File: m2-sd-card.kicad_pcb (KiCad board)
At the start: 4 copper layers, 30 x 22 mm, 16 parts, among them J101 M.2_Key_E, J102 Conn_01x02, J103 Conn_02x03_Counter_Clockwise, J104 Conn_02x03_Counter_Clockwise, J105 Conn_01x01, J106 Conn_01x03, J107 Conn_01x02, J108 USB_B_Micro, J109 Micro_SD, U101 SN74LV1T34DBV

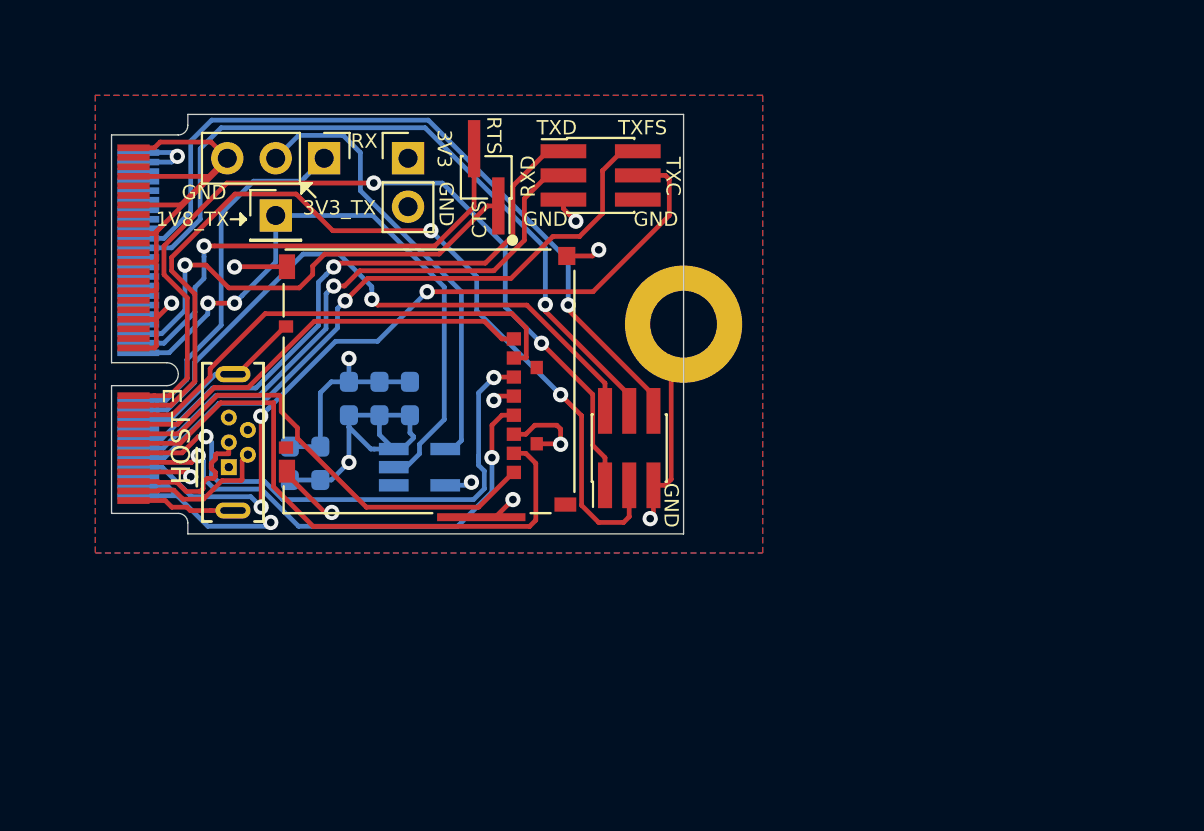
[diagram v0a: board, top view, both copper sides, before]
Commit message: Import all of the footprints into the layout
Delete the traces and footprints from the M.2 breakout board.

Update the design rules constraints and physical stackup using PCBWay's
manufacturing capabilities. These rules should work well for essentially
any manufacturer that ends up being used.

Adjust the NVT4857UK's WLCSP20 footprint according to NXP's recommended
footprint and PCBWay's manufacturing capabilities (allowing for at least
a 4mil soldermask web/bridge between pads). This package's small 0.4mm
pitch makes it so that via-in-pad technology is required for this
board's design.

Create a footprint which contains a MicroSD card 3D Step model and add
it to the board, specifying that it does not exist in the schematic.
This model is used to determine the placement of the MicroSD slot,
making sure that there is sufficient room to insert and remove the
MicroSD card while the M.2 module is installed in the phone. The current
position of x=131.8mm, y=-98.3mm for the DM3AT-SF-PEJM5 MicroSD slot allows
for this to be possible.
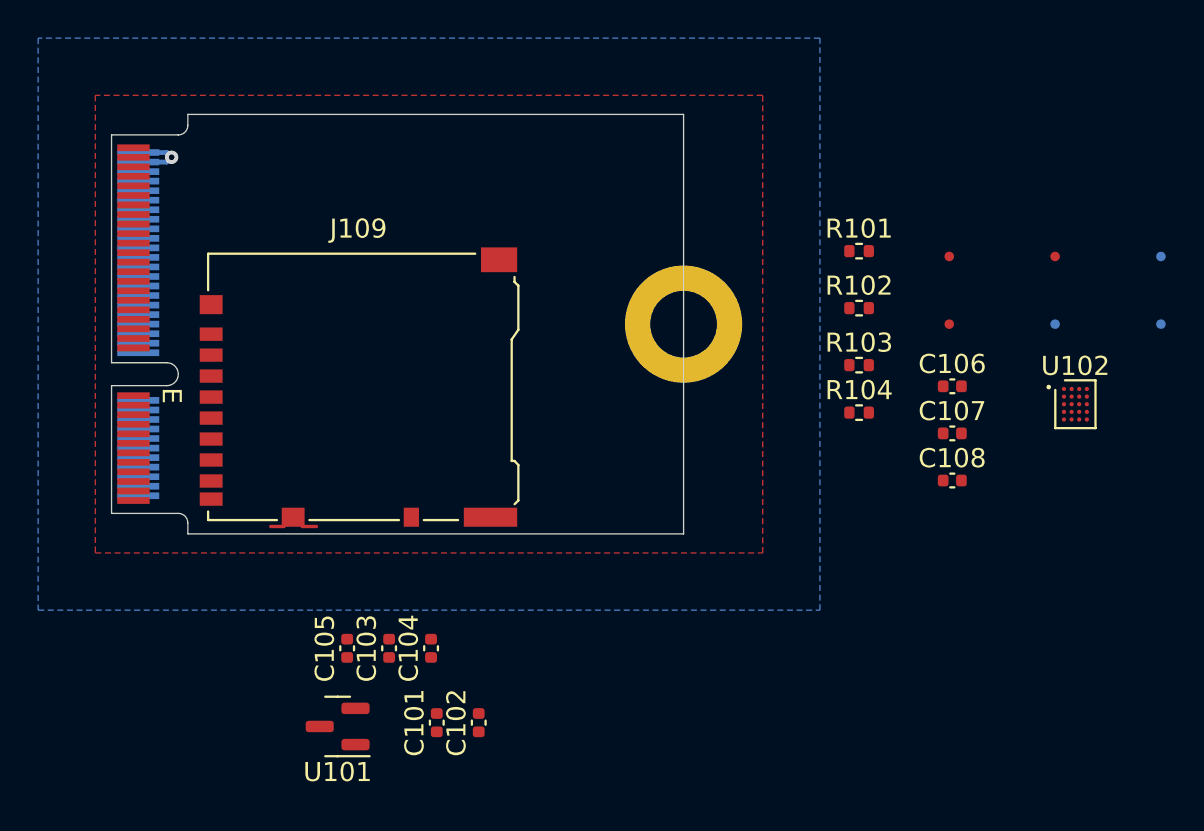
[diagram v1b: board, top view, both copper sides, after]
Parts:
- removed J102: Conn_01x02, Connector_PinHeader_2.54mm:PinHeader_1x02_P2.54mm_Vertical
- removed J103, J104: Conn_02x03_Counter_Clockwise, Connector_PinHeader_1.27mm:PinHeader_2x03_P1.27mm_Vertical_SMD
- removed J105: Conn_01x01, Connector_PinHeader_2.54mm:PinHeader_1x01_P2.54mm_Vertical
- removed J106: Conn_01x03, Connector_PinHeader_2.54mm:PinHeader_1x03_P2.54mm_Vertical
- removed J107: Conn_01x02, Connector_PinHeader_1.27mm:PinHeader_1x02_P1.27mm_Vertical_SMD_Pin1Right
- removed J108: USB_B_Micro, Connector_USB:USB_Micro-B_Wuerth_614105150721_Vertical
- added C106: 100nF, Capacitor_SMD:C_0402_1005Metric, F.Cu at (162.9, 98.3)
- added C107: 1uF, Capacitor_SMD:C_0402_1005Metric, F.Cu at (162.9, 100.7)
- added C108: 2.2uF, Capacitor_SMD:C_0402_1005Metric, F.Cu at (162.9, 103.2)
- added FID101: Fiducial, Fiducial:Fiducial_0.5mm_Mask1mm, F.Cu at (162.8, 91.5)
- added FID102: Fiducial, Fiducial:Fiducial_0.5mm_Mask1mm, F.Cu at (162.8, 95.0)
- added FID103: Fiducial, Fiducial:Fiducial_0.5mm_Mask1mm, F.Cu at (168.3, 91.5)
- added FID104: Fiducial, Fiducial:Fiducial_0.5mm_Mask1mm, B.Cu at (168.3, 95.0)
- added FID105: Fiducial, Fiducial:Fiducial_0.5mm_Mask1mm, B.Cu at (173.9, 91.5)
- added FID106: Fiducial, Fiducial:Fiducial_0.5mm_Mask1mm, B.Cu at (173.9, 95.0)
- added R101: 0, Resistor_SMD:R_0402_1005Metric, F.Cu at (158.1, 91.2)
- added R102: 0, Resistor_SMD:R_0402_1005Metric, F.Cu at (158.1, 94.2)
- added R103: 0, Resistor_SMD:R_0402_1005Metric, F.Cu at (158.1, 97.2)
- added R104: 100k, Resistor_SMD:R_0402_1005Metric, F.Cu at (158.1, 99.6)
- added REF**: MicroSD, m2-sd-card:MicroSD, F.Cu at (131.8, 98.3)
- added U102: NVT4857UK, m2-sd-card:NVT4857UK, F.Cu at (169.4, 99.2)
- C101: value 1u -> 1uF; footprint Capacitor_SMD:C_0603_1608Metric_Pad1.05x0.95mm_HandSolder -> Capacitor_SMD:C_0402_1005Metric; moved to F.Cu
- C102, C103, C104, C105: footprint Capacitor_SMD:C_0603_1608Metric_Pad1.05x0.95mm_HandSolder -> Capacitor_SMD:C_0402_1005Metric; moved to F.Cu
- J109: value Micro_SD -> Micro_SD_Card_Det2; footprint m2-sd-card:ALPS_SCHA4B0419 -> Connector_Card:microSD_HC_Hirose_DM3AT-SF-PEJM5
- U101: value SN74LV1T34DBV -> AP2120N-1.8; footprint Package_TO_SOT_SMD:SOT-23-5_HandSoldering -> Package_TO_SOT_SMD:SOT-23; moved to F.Cu
- moved C102 16.8 mm to (138.1, 115.9)
- moved C101 14.9 mm to (135.9, 115.9)
- moved U101 14.3 mm to (130.7, 116.1), turned to 180 degrees
- moved C104 13.8 mm to (135.6, 112.0)
- moved C105 13.5 mm to (131.2, 112.0)
- moved C103 13.1 mm to (133.4, 112.0)
- moved J109 3.71 mm to (131.8, 98.3)
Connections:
- C101 pad 1: GND -> +3V3
- C101 pad 2: +3V3 -> GND
- C102 pad 1: GND -> +3V3
- C102 pad 2: +3V3 -> GND
- C103 pad 1: GND -> +3V3
- C103 pad 2: +3V3 -> GND
- C104 pad 1: GND -> +3V3
- C104 pad 2: +3V3 -> GND
- C105 pad 1: GND -> +3V3
- C105 pad 2: +3V3 -> GND
- J109 pad 1: /SDIO_DATA2 -> Net-(J109-DAT2)
- J109 pad 2: /SDIO_DATA3 -> Net-(J109-DAT3/CD)
- J109 pad 3: /SDIO_CMD -> Net-(J109-CMD)
- J109 pad 5: /SDIO_CLK -> Net-(J109-CLK)
- J109 pad 7: /SDIO_DATA0 -> Net-(J109-DAT0)
- J109 pad 8: /SDIO_DATA1 -> Net-(J109-DAT1)
- J109 pad 9: unconnected-(J109-DET-Pad9) -> /BT_WAKE
- U101 pad 1: unconnected-(U101-NC-Pad1) -> GND
- U101 pad 2: /SoC_UART_TX -> +1V8
- U101 pad 3: GND -> +3V3
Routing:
- net GND: track 106.2 -> 2.80 mm, vias 10 -> 0
- net /~{SDIO_WAKE}: track 48.8 -> 0.00 mm, vias 2 -> 0
- net /~{SDIO_RST}: track 46.0 -> 0.00 mm, vias 2 -> 0
- net /I2S_TXC: track 41.5 -> 0.00 mm, vias 3 -> 0
- net /WIFI_REG_ON: track 40.1 -> 0.00 mm, vias 1 -> 0
- net /BT_REG_ON: track 39.1 -> 0.00 mm, vias 1 -> 0
- net /I2S_TXFS: track 34.8 -> 0.00 mm, vias 1 -> 0
- net /SoC_UART_TX: track 33.3 -> 0.00 mm, vias 2 -> 0
- net /BT_WAKE: track 33.1 -> 0.00 mm, vias 1 -> 0
- net /SDIO_DATA0: track 31.7 -> 0.00 mm
- net /I2S_TXD: track 31.4 -> 0.00 mm, vias 1 -> 0
- net /I2S_RXD: track 30.6 -> 0.00 mm, vias 1 -> 0
- net /SDIO_CMD: track 29.0 -> 0.00 mm, vias 2 -> 0
- net /SDIO_CLK: track 26.6 -> 0.00 mm, vias 2 -> 0
- net /SDIO_DATA3: track 25.6 -> 0.00 mm
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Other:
- rule pad_to_mask_clearance: 0.01 -> 0.052
- rule solder_mask_min_width: 0.25 -> 0.1016
- board text added: "M.2 μSD Card"
- board text removed: "1V8_TX"
- board text removed: "3V3"
- board text removed: "3V3_TX"
- board text removed: "CTS"
- board text removed: "GND"
- board text removed: "HOST"
- board text removed: "M.2 Breakout"
- board text removed: "RTS"
- board text removed: "RX"
- board text removed: "RXD"
- board text removed: "TXC"
- board text removed: "TXD"
- board text removed: "TXFS"

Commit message: Hook up all of the nets and make sure DRC is passing
Exceptions were made for the half-mounting hole and a silkscreen overlap
with C3.

Reset the reference designators to first free number starting at 0 so
that they take up less space on the silkscreen.

Layout is not completely done and still needs to be polished up.
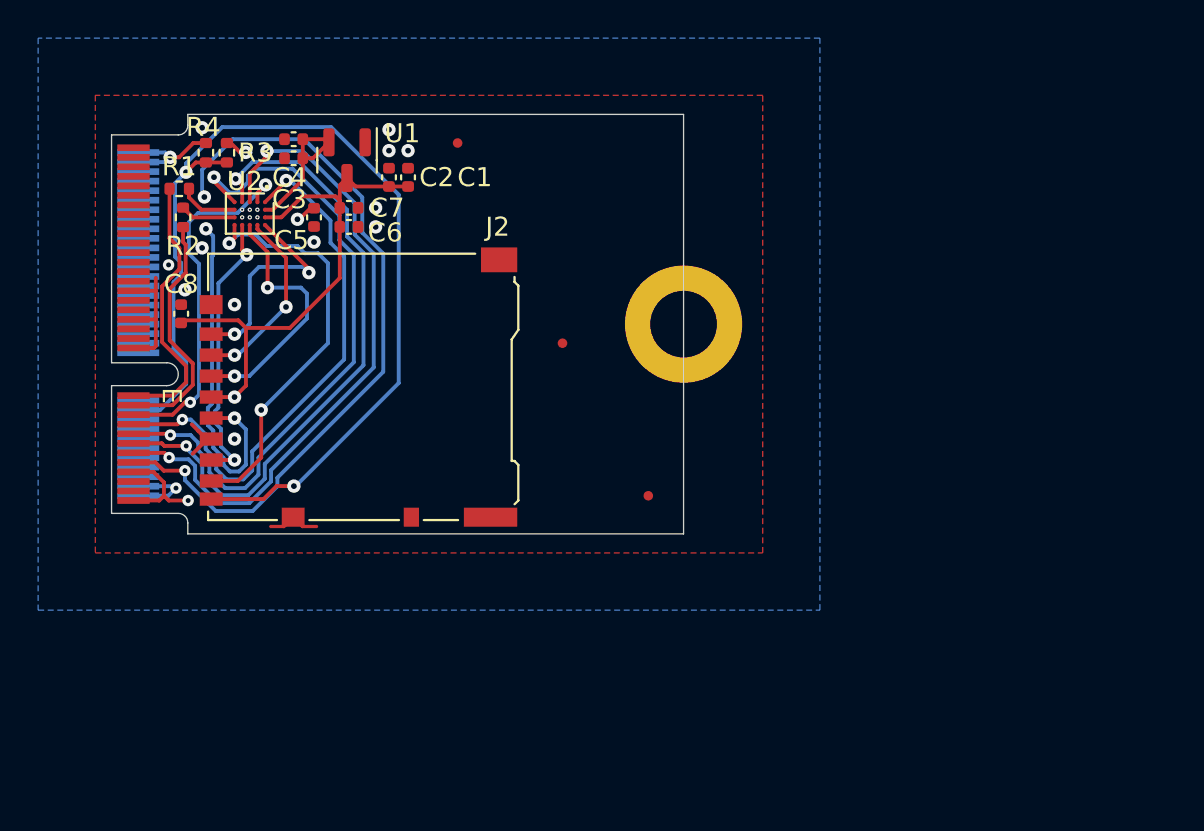
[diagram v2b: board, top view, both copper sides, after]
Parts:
- removed FID104, FID105, FID106: Fiducial, Fiducial:Fiducial_0.5mm_Mask1mm
- moved U2 44.4 mm to (126.1, 89.2), turned to -90 degrees
- moved C4 37.8 mm to (128.4, 85.3), turned to 180 degrees
- moved R4 36.9 mm to (123.8, 86.0), turned to -90 degrees
- moved C3 36.6 mm to (128.4, 86.3), turned to 180 degrees
- moved C5 36.2 mm to (129.5, 89.4), turned to -90 degrees
- moved R1 35.8 mm to (122.4, 87.9)
- moved R2 35.8 mm to (122.6, 89.4), turned to 90 degrees
- moved R3 35.0 mm to (124.9, 86.0), turned to -90 degrees
- moved U1 29.7 mm to (131.2, 86.4), turned to -90 degrees
- moved C2 29.0 mm to (133.4, 87.3)
- moved C1 28.6 mm to (134.4, 87.3)
- moved FID1 26.5 mm to (137.0, 85.5)
- moved FID3 26.2 mm to (142.5, 96.0)
- moved C7 23.5 mm to (131.3, 88.9), turned to 0 degrees
- moved C6 22.2 mm to (131.3, 89.9), turned to 0 degrees
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- renumbered C101 to C1, C102 to C2, C106 to C3, C107 to C4, C108 to C5, C103 to C6, C104 to C7, C105 to C8, FID101 to FID1, FID102 to FID2, FID103 to FID3, H101 to H1, J101 to J1, J109 to J2, R101 to R1, R102 to R2, R103 to R3, R104 to R4, U101 to U1, U102 to U2
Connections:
- R1 pad 1: /~{SDIO_WAKE} -> /~{SDIO_RST}
- R2 pad 1: /~{SDIO_RST} -> /~{SDIO_WAKE}
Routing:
- net +3V3: track 3.71 -> 60.1 mm, vias 1 -> 3
- net /BT_WAKE: track 0.00 -> 53.5 mm, vias 0 -> 2
- net /SDIO_CLK: track 0.00 -> 41.4 mm, vias 0 -> 3
- net /SDIO_CMD: track 0.00 -> 35.2 mm, vias 0 -> 2
- net /SDIO_DATA1: track 0.00 -> 35.0 mm, vias 0 -> 2
- net /SDIO_DATA0: track 0.00 -> 34.0 mm, vias 0 -> 2
- net /SDIO_DATA2: track 0.00 -> 28.7 mm, vias 0 -> 2
- net Net-(J2-DAT1): track 0.00 -> 21.8 mm, vias 0 -> 2
- net Net-(J2-CLK): track 0.00 -> 20.5 mm, vias 0 -> 3
- net /SDIO_DATA3: track 0.00 -> 18.8 mm, vias 0 -> 2
- net GND: track 2.80 -> 18.2 mm, vias 0 -> 15
- net Net-(J2-DAT0): track 0.00 -> 14.8 mm, vias 0 -> 2
- net /~{SDIO_RST}: track 0.00 -> 14.3 mm
- net Net-(J2-CMD): track 0.00 -> 13.4 mm, vias 0 -> 2
- net /~{SDIO_WAKE}: track 0.00 -> 12.7 mm
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- added copper zone on In2.Cu, net GND
- removed copper zone on In2.Cu, net +3V3

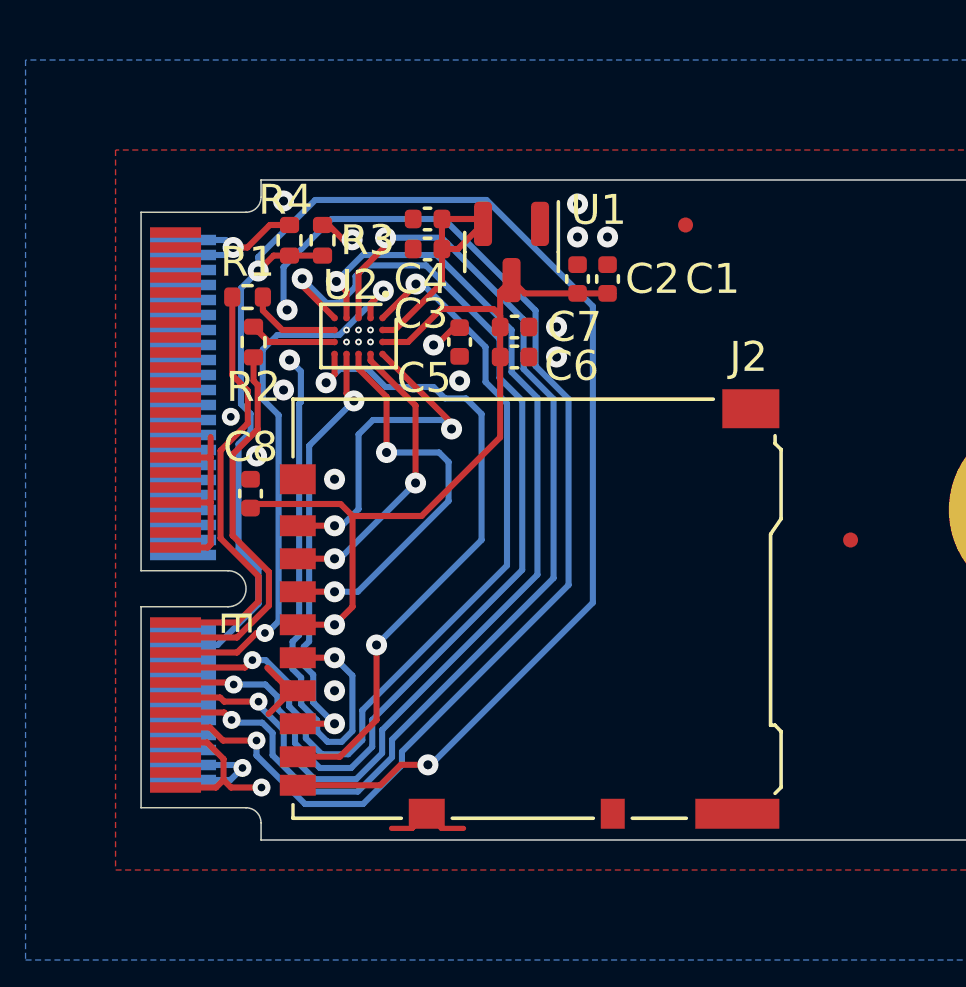
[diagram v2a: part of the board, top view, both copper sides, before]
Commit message: Finish the routing of the board and export the gerbers and all manufacturing files
Add fab notes to the layout.

Generate a fabrication drawing and include it in the gerbers directory
since that is the location PCBWay will use (when this directory's
contents are archived into a zip).

Export the 3D step model of the board.

Export the IPC-D-356 netlist file which will be used to verify the
gerbers.
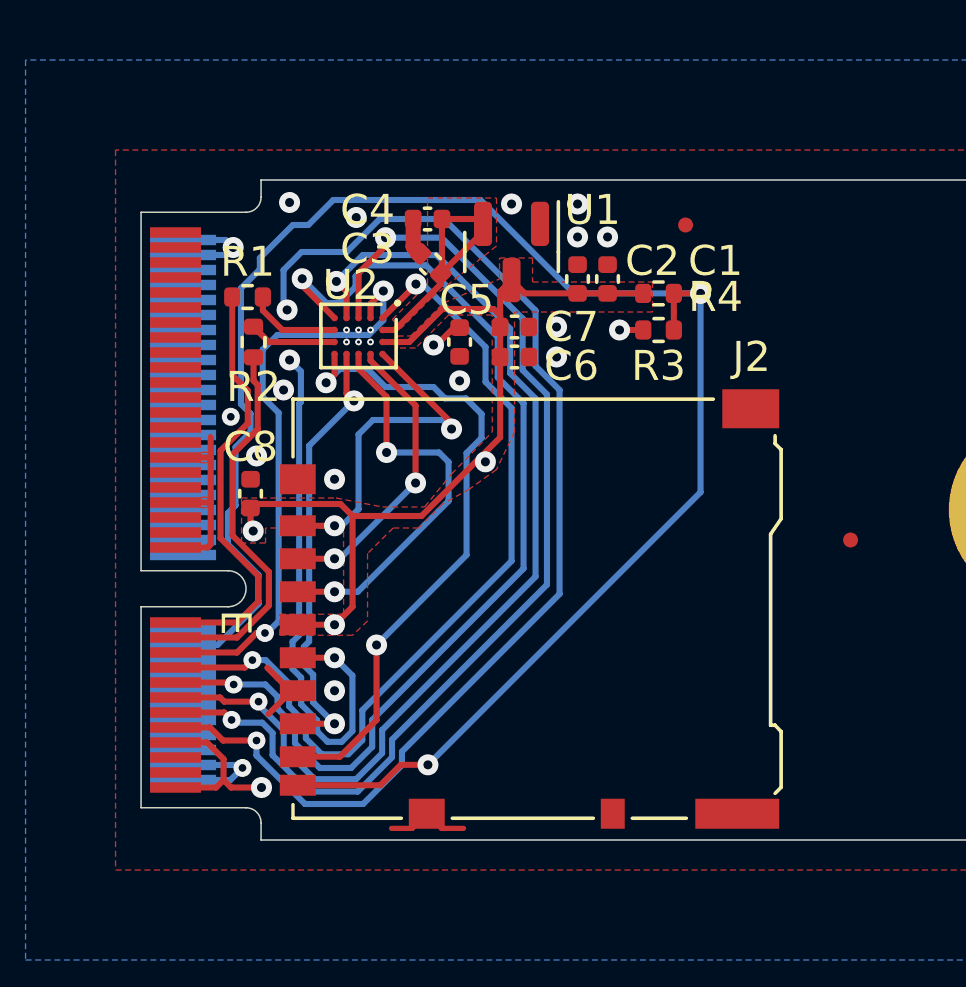
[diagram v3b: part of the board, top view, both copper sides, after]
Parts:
- moved R4 12.4 mm to (136.1, 87.8), turned to 0 degrees
- moved R3 11.6 mm to (136.1, 89.0), turned to 0 degrees
- moved FID2 9.18 mm to (142.5, 96.0)
- moved FID3 9.18 mm to (147.0, 104.0)
- moved C3 0.51 mm to (128.5, 86.8), turned to 135 degrees
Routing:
- net +3V3: track 60.1 -> 68.1 mm, vias 3 -> 5
- net /BT_WAKE: track 53.5 -> 58.7 mm
- net Net-(U2-CD): track 11.3 -> 9.92 mm
- net GND: track 18.2 -> 19.4 mm, vias 15 -> 17
- net /SDIO_DATA3: track 18.8 -> 19.3 mm
- net +1V8: track 7.91 -> 8.46 mm
- added copper zone on F.Cu, net +1V8
- added copper zone on F.Cu, net +3V3
- added copper zone on In1.Cu, net +3V3
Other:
- board text added: "0"
- board text added: "0 mm"
- board text added: "0.01 mm"
- board text added: "0.02"
- board text added: "0.035 mm"
- board text added: "0.11 mm"
- board text added: "0.1270 mm / 0.1270 mm"
- board text added: "0.2540 mm"
- board text added: "0.4 mm"
- board text added: "0.7800 mm"
- board text added: "1"
- board text added: "1. THIS BOARD SHALL CONFORM TO: IPC-6012, CURRENT REVISION, CLASS II IPC-A-600, CURRENT REVISION, CLASS II 2. OVERALL BOARD THICKNESS SHALL BE 0.80mm +/-10%. 3. MATERIAL SHALL BE IT180A OR EQUIVALENT. 4. SEE SUPPLEMENTARY PDF DOCUMENT FOR STACKUP COMPOSITION AND IMPEDANCE REQUIREMENTS. 5. USE SUPPLIED IPC-D-356 NETLIST TO PERFORM COMPARISON WITH GERBER DATA PRIOR TO MANUFACTURING. 6. APPLY SOLDER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"
- board text added: "3.3"
- board text added: "30.0000 mm x 22.0000 mm"
- board text added: "4"
- board text added: "4.29"
- board text added: "B.Cu"
- board text added: "B.Mask"
- board text added: "B.Paste"
- board text added: "B.Silkscreen"
- board text added: "BOARD CHARACTERISTICS"
- board text added: "Board Thickness:"
- board text added: "Board overall dimensions:"
- board text added: "Bottom Silk Screen"
- board text added: "Bottom Solder Mask"
- board text added: "Bottom Solder Paste"
- board text added: "Castellated pads:"
- board text added: "Color"
- board text added: "Copper Finish:"
- board text added: "Copper Layer Count:"
- board text added: "Dielectric"
- board text added: "ENIG"
- board text added: "Edge card connectors:"
- board text added: "Epoxy"
- board text added: "Epsilon R"
- board text added: "F.Cu"
- board text added: "F.Mask"
- board text added: "F.Paste"
- board text added: "F.Silkscreen"
- board text added: "FR4"
- board text added: "FR4 natural"
- board text added: "Green"
- board text added: "Impedance Control:"
- board text added: "In1.Cu"
- board text added: "In2.Cu"
- board text added: "Layer Name"
- board text added: "Liquid Photo"
- board text added: "Loss Tangent"
- board text added: "Material"
- board text added: "Min hole diameter:"
- board text added: "Min track/spacing:"
- board text added: "NOTE: UNLESS OTHERWISE SPECIFIED"
- board text added: "No"
- board text added: "PP2116"
- board text added: "Plated Board Edge:"
- board text added: "Purism SPC GPLv3+"
- board text added: "Thickness (mm)"
- board text added: "Top Silk Screen"
- board text added: "Top Solder Mask"
- board text added: "Top Solder Paste"
- board text added: "Type"
- board text added: "White"
- board text added: "Yes"
- board text added: "copper"
- board text added: "core"
- board text added: "prepreg"
- board text removed: "Purism SPC GNU GPLv3+"
